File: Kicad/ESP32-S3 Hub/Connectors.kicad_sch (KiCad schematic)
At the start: 23 parts, among them J1 1.27mm 3pin socket, J10 1.27mm 3pin socket, J11 7 pin FPC 0.3mm Panasonic Y3b, J12 1.27mm 3pin socket, J13 TE 3-2363961-0 receptacle, J14 TE 3-2363962-0 Connector, J16 TE 3-2363961-0 receptacle, J17 TE 3-2363962-0 Connector, J2 1.27mm 3pin socket, J21 1.27mm 4 pin socket, J22 1.27mm 4 pin header, J3 7 pin FPC 0.3mm Panasonic Y3b, J4 1.27mm 3pin socket, J5 7 pin FPC 0.3mm Panasonic Y3b, J6 1.27mm 3pin socket, J7 1.27mm 3pin socket, J8 7 pin FPC 0.3mm Panasonic Y3b, J9 1.27mm 3pin socket

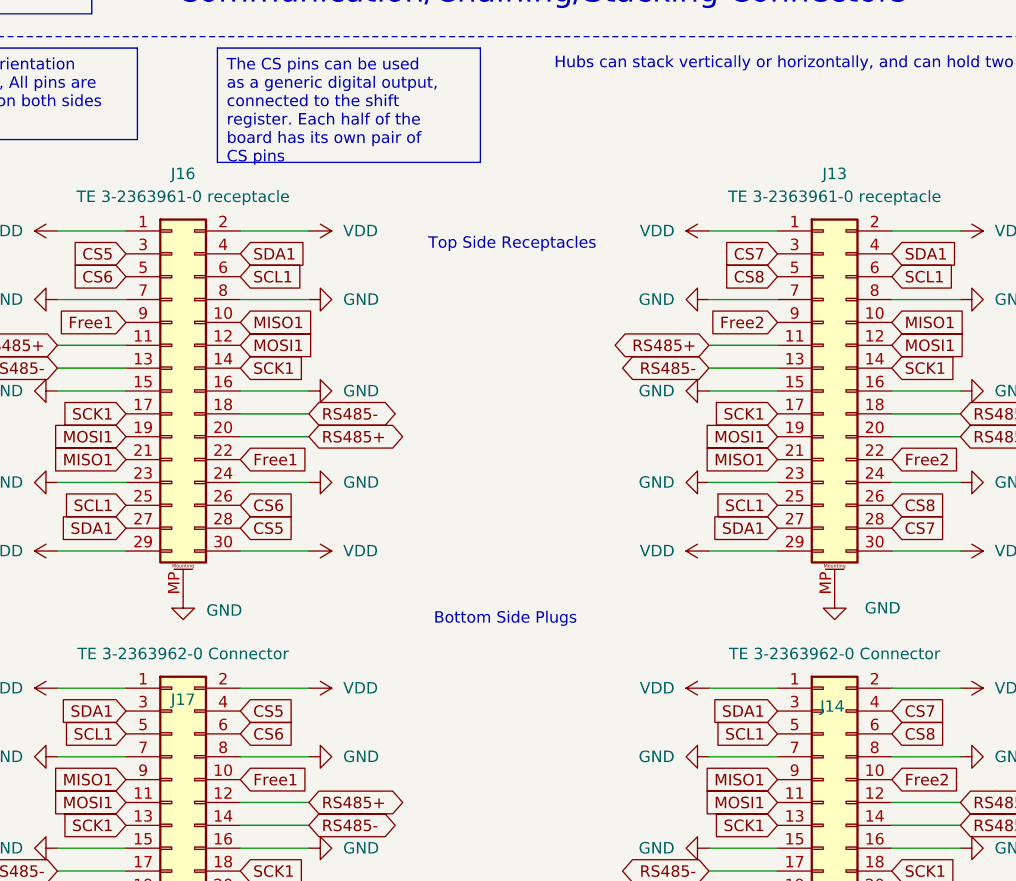
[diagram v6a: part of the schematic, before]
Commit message: Swapped header logical numbers
I realized my numbering scheme was off with the actual board layout. So in the schematic I swapped the connectors without rewiring so that the numbers are more logical. CS7, CS8, and Free2 are now for the top mezzanine connector, which is closer to the pins on the chips. It also falls in line with my bottom up numbering scheme.
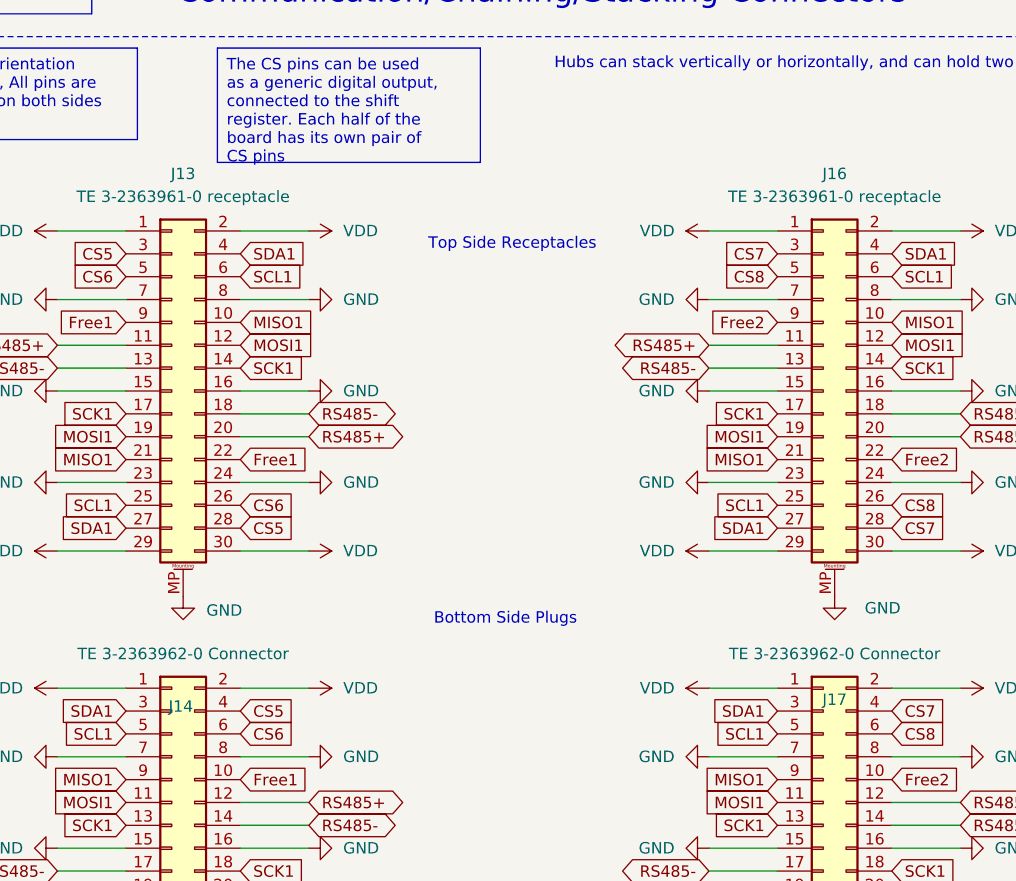
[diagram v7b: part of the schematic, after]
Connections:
- net CS5: now also J13.28 (Pin_28), J13.3 (Pin_3), J14.27 (Pin_27), J14.4 (Pin_4); no longer J16.28 (Pin_28), J16.3 (Pin_3), J17.27 (Pin_27), J17.4 (Pin_4)
- net CS6: now also J13.26 (Pin_26), J13.5 (Pin_5), J14.25 (Pin_25), J14.6 (Pin_6); no longer J16.26 (Pin_26), J16.5 (Pin_5), J17.25 (Pin_25), J17.6 (Pin_6)
- net CS7: now also J16.28 (Pin_28), J16.3 (Pin_3), J17.27 (Pin_27), J17.4 (Pin_4); no longer J13.28 (Pin_28), J13.3 (Pin_3), J14.27 (Pin_27), J14.4 (Pin_4)
- net CS8: now also J16.26 (Pin_26), J16.5 (Pin_5), J17.25 (Pin_25), J17.6 (Pin_6); no longer J13.26 (Pin_26), J13.5 (Pin_5), J14.25 (Pin_25), J14.6 (Pin_6)
- net Free1: now also J13.22 (Pin_22), J13.9 (Pin_9), J14.10 (Pin_10), J14.21 (Pin_21); no longer J16.22 (Pin_22), J16.9 (Pin_9), J17.10 (Pin_10), J17.21 (Pin_21)
- net Free2: now also J16.22 (Pin_22), J16.9 (Pin_9), J17.10 (Pin_10), J17.21 (Pin_21); no longer J13.22 (Pin_22), J13.9 (Pin_9), J14.10 (Pin_10), J14.21 (Pin_21)
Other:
- moved on the sheet: J13, J14, J16, J17
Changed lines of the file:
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@@
+	(symbol
+		(lib_id "Connector_Generic_MountingPin:Conn_02x15_Odd_Even_MountingPin")
+		(at 173.99 142.24 0)
+		(unit 1)
+		(exclude_from_sim no)
+		(in_bom yes)
+		(on_board yes)
+		(dnp no)
+		(property "Reference" "J14"
+			(at 175.006 126.492 0)
+			(effects
+				(font
+					(size 1.27 1.27)
+				)
+			)
+		)
+		(property "Value" "TE 3-2363962-0 Connector"
+			(at 175.26 120.65 0)
+			(effects
+				(font
+					(size 1.27 1.27)
+				)
+			)
+		)
+		(property "Footprint" "custom_testpoints:TE_mezzanine_conn_3-2363962-0"
+			(at 173.99 142.24 0)
+			(effects
+				(font
+					(size 1.27 1.27)
+				)
+				(hide yes)
+			)
+		)
+		(property "Datasheet" "~"
+			(at 173.99 142.24 0)
+			(effects
+				(font
+					(size 1.27 1.27)
+				)
+				(hide yes)
+			)
+		)
+		(property "Description" "Generic connectable mounting pin connector, double row, 02x15, odd/even pin numbering scheme (row 1 odd numbers, row 2 even numbers), script generated (kicad-library-utils/schlib/autogen/connector/)"
+			(at 173.99 142.24 0)
+			(effects
+				(font
+					(size 1.27 1.27)
+				)
+				(hide yes)
+			)
+		)
+		(pin "28"
+		)
+		(pin "21"
+		)
+		(pin "25"
+		)
+		(pin "5"
+		)
+		(pin "17"
+		)
+		(pin "6"
+		)
+		(pin "14"
+		)
+		(pin "2"
+		)
+		(pin "24"
+		)
+		(pin "8"
+		)
+		(pin "30"
+		)
+		(pin "23"
+		)
+		(pin "16"
+		)
+		(pin "19"
+		)
+		(pin "22"
+		)
+		(pin "7"
+		)
+		(pin "3"
+		)
+		(pin "9"
+		)
+		(pin "MP"
+		)
+		(pin "4"
+		)
+		(pin "27"
+		)
+		(pin "29"
+		)
+		(pin "26"
+		)
+		(pin "18"
+		)
+		(pin "20"
+		)
+		(pin "13"
+		)
+		(pin "10"
+		)
+		(pin "12"
+		)
+		(pin "11"
+		)
+		(pin "1"
+		)
+		(pin "15"
+		)
+		(instances
+			(project "ESP32-S3 Hub"
+				(path "/a8c80fba-3bca-4358-b5bb-9ebf9383c658/e098af34-1b04-4f22-87f1-2a3ef3b390de"
+					(reference "J14")
+					(unit 1)
+				)
+			)
+		)
+	)
+	(symbol
+		(lib_id "Device:R_Small")
+		(at 69.85 97.79 0)
+		(unit 1)
+		(exclude_from_sim no)
+		(in_bom yes)
+		(on_board yes)
+		(dnp no)
+		(property "Reference" "R19"
+			(at 71.12 101.346 0)
+			(effects
+				(font
+					(size 1.27 1.27)
+				)
+			)
+		)
+		(property "Value" "10k"
+			(at 66.548 98.044 0)
+			(effects
+				(font
+					(size 1.27 1.27)
+				)
+			)
+		)
+		(property "Footprint" "Resistor_SMD:R_0402_1005Metric"
+			(at 69.85 97.79 0)
+			(effects
+				(font
+					(size 1.27 1.27)
+				)
+				(hide yes)
+			)
+		)
+		(property "Datasheet" "~"
+			(at 69.85 97.79 0)
+			(effects
+				(font
+					(size 1.27 1.27)
+				)
+				(hide yes)
+			)
+		)
+		(property "Description" "Resistor, small symbol"
+			(at 69.85 97.79 0)
+			(effects
+				(font
+					(size 1.27 1.27)
+				)
+				(hide yes)
+			)
+		)
+		(pin "2"
+		)
+		(pin "1"
+		)
+		(instances
+			(project "ESP32-S3 Hub"
+				(path "/a8c80fba-3bca-4358-b5bb-9ebf9383c658/e098af34-1b04-4f22-87f1-2a3ef3b390de"
+					(reference "R19")
+					(unit 1)
+				)
+			)
+		)
+	)
 	(symbol
 		(lib_id "Connector_Generic_MountingPin:Conn_02x15_Odd_Even_MountingPin")
@@
 		(on_board yes)
 		(dnp no)
-		(property "Reference" "J14"
-			(at 247.396 126.492 0)
+		(property "Reference" "J17"
+			(at 247.65 125.73 0)
 			(effects
 				(font
@@
 		(property "Description" "Generic connectable mounting pin connector, double row, 02x15, odd/even pin numbering scheme (row 1 odd numbers, row 2 even numbers), script generated (kicad-library-utils/schlib/autogen/connector/)"
 			(at 246.38 142.24 0)
-			(effects
-				(font
-					(size 1.27 1.27)
-				)
-				(hide yes)
-			)
-		)
-		(pin "28"
-		)
-		(pin "21"
-		)
-		(pin "25"
-		)
-		(pin "5"
-		)
-		(pin "17"
-		)
-		(pin "6"
-		)
-		(pin "14"
-		)
-		(pin "2"
-		)
-		(pin "24"
-		)
-		(pin "8"
-		)
-		(pin "30"
-		)
-		(pin "23"
-		)
-		(pin "16"
-		)
-		(pin "19"
-		)
-		(pin "22"
-		)
-		(pin "7"
-		)
-		(pin "3"
-		)
-		(pin "9"
-		)
-		(pin "MP"
-		)
-		(pin "4"
-		)
-		(pin "27"
-		)
-		(pin "29"
-		)
-		(pin "26"
-		)
-		(pin "18"
-		)
-		(pin "20"
-		)
-		(pin "13"
-		)
-		(pin "10"
-		)
-		(pin "12"
-		)
-		(pin "11"
-		)
-		(pin "1"
-		)
-		(pin "15"
-		)
-		(instances
-			(project "ESP32-S3 Hub"
-				(path "/a8c80fba-3bca-4358-b5bb-9ebf9383c658/e098af34-1b04-4f22-87f1-2a3ef3b390de"
-					(reference "J14")
-					(unit 1)
-				)
-			)
-		)
-	)
-	(symbol
-		(lib_id "Device:R_Small")
-		(at 69.85 97.79 0)
-		(unit 1)
-		(exclude_from_sim no)
-		(in_bom yes)
-		(on_board yes)
-		(dnp no)
-		(property "Reference" "R19"
-			(at 71.12 101.346 0)
-			(effects
-				(font
-					(size 1.27 1.27)
-				)
-			)
-		)
-		(property "Value" "10k"
-			(at 66.548 98.044 0)
-			(effects
-				(font
-					(size 1.27 1.27)
-				)
-			)
-		)
-		(property "Footprint" "Resistor_SMD:R_0402_1005Metric"
-			(at 69.85 97.79 0)
-			(effects
-				(font
-					(size 1.27 1.27)
-				)
-				(hide yes)
-			)
-		)
-		(property "Datasheet" "~"
-			(at 69.85 97.79 0)
-			(effects
-				(font
-					(size 1.27 1.27)
-				)
-				(hide yes)
-			)
-		)
-		(property "Description" "Resistor, small symbol"
-			(at 69.85 97.79 0)
-			(effects
-				(font
-					(size 1.27 1.27)
-				)
-				(hide yes)
-			)
-		)
-		(pin "2"
-		)
-		(pin "1"
-		)
-		(instances
-			(project "ESP32-S3 Hub"
-				(path "/a8c80fba-3bca-4358-b5bb-9ebf9383c658/e098af34-1b04-4f22-87f1-2a3ef3b390de"
-					(reference "R19")
-					(unit 1)
-				)
-			)
-		)
-	)
-	(symbol
-		(lib_id "Connector_Generic_MountingPin:Conn_02x15_Odd_Even_MountingPin")
-		(at 173.99 142.24 0)
-		(unit 1)
-		(exclude_from_sim no)
-		(in_bom yes)
-		(on_board yes)
-		(dnp no)
-		(property "Reference" "J17"
-			(at 175.26 125.73 0)
-			(effects
-				(font
-					(size 1.27 1.27)
-				)
-			)
-		)
-		(property "Value" "TE 3-2363962-0 Connector"
-			(at 175.26 120.65 0)
-			(effects
-				(font
-					(size 1.27 1.27)
-				)
-			)
-		)
-		(property "Footprint" "custom_testpoints:TE_mezzanine_conn_3-2363962-0"
-			(at 173.99 142.24 0)
-			(effects
-				(font
-					(size 1.27 1.27)
-				)
-				(hide yes)
-			)
-		)
-		(property "Datasheet" "~"
-			(at 173.99 142.24 0)
-			(effects
-				(font
-					(size 1.27 1.27)
-				)
-				(hide yes)
-			)
-		)
-		(property "Description" "Generic connectable mounting pin connector, double row, 02x15, odd/even pin numbering scheme (row 1 odd numbers, row 2 even numbers), script generated (kicad-library-utils/schlib/autogen/connector/)"
-			(at 173.99 142.24 0)
 			(effects
 				(font
@@
 	(symbol
 		(lib_id "Connector_Generic_MountingPin:Conn_02x15_Odd_Even_MountingPin")
-		(at 246.38 91.44 0)
+		(at 173.99 91.44 0)
 		(unit 1)
 		(exclude_from_sim no)
@@
 		(fields_autoplaced yes)
 		(property "Reference" "J13"
-			(at 247.65 67.31 0)
+			(at 175.26 67.31 0)
 			(effects
 				(font
@@
 		)
 		(property "Value" "TE 3-2363961-0 receptacle"
-			(at 247.65 69.85 0)
+			(at 175.26 69.85 0)
 			(effects
 				(font
@@
 		)
 		(property "Footprint" "custom_testpoints:TE_mezzanine_rec_3-2363961-0"
-			(at 246.38 91.44 0)
+			(at 173.99 91.44 0)
 			(effects
 				(font
@@
 		)
 		(property "Datasheet" "~"
-			(at 246.38 91.44 0)
+			(at 173.99 91.44 0)
 			(effects
 				(font
@@
 		)
 		(property "Description" "Generic connectable mounting pin connector, double row, 02x15, odd/even pin numbering scheme (row 1 odd numbers, row 2 even numbers), script generated (kicad-library-utils/schlib/autogen/connector/)"
-			(at 246.38 91.44 0)
+			(at 173.99 91.44 0)
 			(effects
 				(font
@@
 	(symbol
 		(lib_id "Connector_Generic_MountingPin:Conn_02x15_Odd_Even_MountingPin")
-		(at 173.99 91.44 0)
+		(at 246.38 91.44 0)
 		(unit 1)
 		(exclude_from_sim no)
@@
 		(fields_autoplaced yes)
 		(property "Reference" "J16"
-			(at 175.26 67.31 0)
+			(at 247.65 67.31 0)
 			(effects
 				(font
@@
 		)
 		(property "Value" "TE 3-2363961-0 receptacle"
-			(at 175.26 69.85 0)
+			(at 247.65 69.85 0)
 			(effects
 				(font
@@
 		)
 		(property "Footprint" "custom_testpoints:TE_mezzanine_rec_3-2363961-0"
-			(at 173.99 91.44 0)
+			(at 246.38 91.44 0)
 			(effects
 				(font
@@
 		)
 		(property "Datasheet" "~"
-			(at 173.99 91.44 0)
+			(at 246.38 91.44 0)
 			(effects
 				(font
@@
 		)
 		(property "Description" "Generic connectable mounting pin connector, double row, 02x15, odd/even pin numbering scheme (row 1 odd numbers, row 2 even numbers), script generated (kicad-library-utils/schlib/autogen/connector/)"
-			(at 173.99 91.44 0)
-			(effects
-				(font
+			(at 246.38 91.44 0)
+			(effects
+				(font

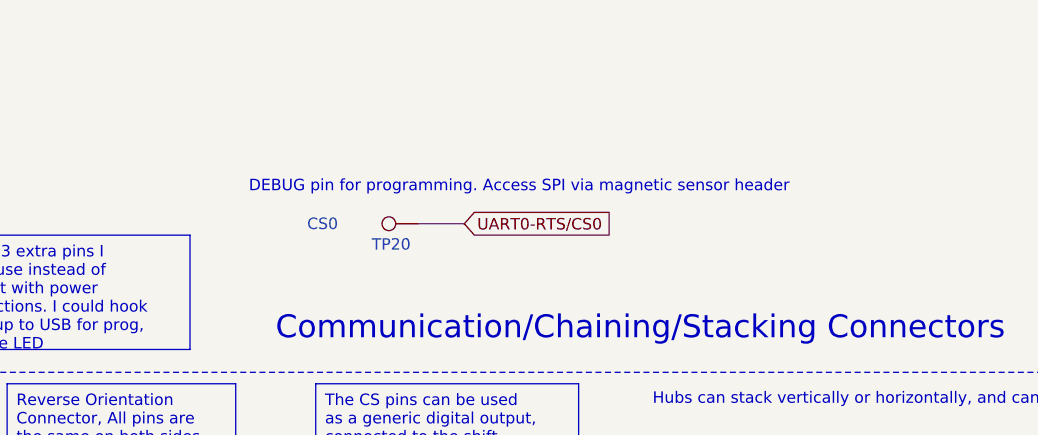
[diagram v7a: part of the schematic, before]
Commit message: Finished basic routing
Now I have to fix some things to try and reduce crosstalk, and improve signal integrity. The likelihood of me being able to completely fix it is low, due to limited space. I also have to run the DRC, and fix the silkscreen.
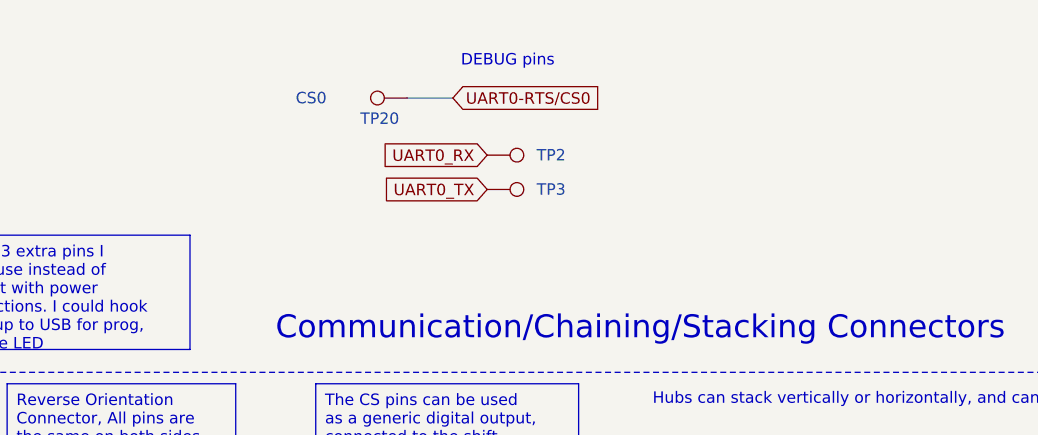
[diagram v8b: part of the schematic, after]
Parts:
- added TP2, TP3: ~, TestPoint:TestPoint_Pad_D1.0mm, symbol Connector:TestPoint
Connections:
- new net UART0_RX: TP2.1
- new net UART0_TX: TP3.1
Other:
- note added: "DEBUG pins"
- note removed: "DEBUG pin for programming. Access SPI via magnetic sensor header"
- moved on the sheet: TP20
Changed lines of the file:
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@@
 	(wire
 		(pts
-			(xy 195.58 35.56) (xy 190.5 35.56)
+			(xy 194.31 21.59) (xy 189.23 21.59)
 		)
 		(stroke
@@
 		)
 	)
-	(text "DEBUG pin for programming. Access SPI via magnetic sensor header"
+	(text "DEBUG pins"
 		(exclude_from_sim no)
-		(at 201.676 31.496 0)
+		(at 200.406 17.526 0)
 		(effects
 			(font
@@
 		)
 	)
+	(global_label "UART0_RX"
+		(shape input)
+		(at 198.12 27.94 180)
+		(fields_autoplaced yes)
+		(effects
+			(font
+				(size 1.27 1.27)
+			)
+			(justify right)
+		)
+		(property "Intersheetrefs" "${INTERSHEET_REFS}"
+			(at 185.8215 27.94 0)
+			(effects
+				(font
+					(size 1.27 1.27)
+				)
+				(justify right)
+				(hide yes)
+			)
+		)
+	)
 	(global_label "SCL1"
 		(shape input)
@@
 		)
 	)
+	(global_label "UART0_TX"
+		(shape input)
+		(at 198.12 31.75 180)
+		(fields_autoplaced yes)
+		(effects
+			(font
+				(size 1.27 1.27)
+			)
+			(justify right)
+		)
+		(property "Intersheetrefs" "${INTERSHEET_REFS}"
+			(at 186.1239 31.75 0)
+			(effects
+				(font
+					(size 1.27 1.27)
+				)
+				(justify right)
+				(hide yes)
+			)
+		)
+	)
 	(global_label "RS485-"
 		(shape bidirectional)
@@
 	(global_label "UART0-RTS{slash}CS0"
 		(shape input)
-		(at 195.58 35.56 0)
+		(at 194.31 21.59 0)
 		(fields_autoplaced yes)
 		(effects
@@
 		)
 		(property "Intersheetrefs" "${INTERSHEET_REFS}"
-			(at 214.4704 35.56 0)
+			(at 213.2004 21.59 0)
 			(effects
 				(font
@@
 	(symbol
 		(lib_id "Connector:TestPoint")
-		(at 190.5 35.56 90)
+		(at 189.23 21.59 90)
 		(unit 1)
 		(exclude_from_sim no)
@@
 		(dnp no)
 		(property "Reference" "TP20"
-			(at 187.452 37.846 90)
+			(at 186.182 23.876 90)
 			(effects
 				(font
@@
 		)
 		(property "Value" "CS0"
-			(at 179.832 35.56 90)
+			(at 178.562 21.59 90)
 			(effects
 				(font
@@
 		)
 		(property "Footprint" "TestPoint:TestPoint_Pad_D1.0mm"
-			(at 190.5 30.48 0)
+			(at 189.23 16.51 0)
 			(effects
 				(font
@@
 		)
 		(property "Datasheet" "~"
-			(at 190.5 30.48 0)
+			(at 189.23 16.51 0)
 			(effects
 				(font
@@
 		)
 		(property "Description" "test point"
-			(at 190.5 35.56 0)
+			(at 189.23 21.59 0)
 			(effects
 				(font
@@
 	)
 	(symbol
+		(lib_id "Connector:TestPoint")
+		(at 198.12 31.75 270)
+		(unit 1)
+		(exclude_from_sim no)
+		(in_bom no)
+		(on_board yes)
+		(dnp no)
+		(property "Reference" "TP3"
+			(at 205.232 31.75 90)
+			(effects
+				(font
+					(size 1.27 1.27)
+				)
+			)
+		)
+		(property "Value" "~"
+			(at 207.01 32.004 90)
+			(effects
+				(font
+					(size 1.27 1.27)
+				)
+			)
+		)
+		(property "Footprint" "TestPoint:TestPoint_Pad_D1.0mm"
+			(at 198.12 36.83 0)
+			(effects
+				(font
+					(size 1.27 1.27)
+				)
+				(hide yes)
+			)
+		)
+		(property "Datasheet" "~"
+			(at 198.12 36.83 0)
+			(effects
+				(font
+					(size 1.27 1.27)
+				)
+				(hide yes)
+			)
+		)
+		(property "Description" "test point"
+			(at 198.12 31.75 0)
+			(effects
+				(font
+					(size 1.27 1.27)
+				)
+				(hide yes)
+			)
+		)
+		(pin "1"
+		)
+		(instances
+			(project "ESP32-S3 Hub"
+				(path "/a8c80fba-3bca-4358-b5bb-9ebf9383c658/e098af34-1b04-4f22-87f1-2a3ef3b390de"
+					(reference "TP3")
+					(unit 1)
+				)
+			)
+		)
+	)
+	(symbol
 		(lib_id "power:GND")
 		(at 162.56 187.96 90)
@@
 					(unit 1)
 				)
+			)
+		)
+	)
+	(symbol
+		(lib_id "Connector:TestPoint")
+		(at 198.12 27.94 270)
+		(unit 1)
+		(exclude_from_sim no)
+		(in_bom no)
+		(on_board yes)
+		(dnp no)
+		(property "Reference" "TP2"
+			(at 205.232 27.94 90)
+			(effects
+				(font
+					(size 1.27 1.27)
+				)
+			)
+		)
+		(property "Value" "~"
+			(at 207.01 28.194 90)
+			(effects
+				(font
+					(size 1.27 1.27)
+				)
+			)
+		)
+		(property "Footprint" "TestPoint:TestPoint_Pad_D1.0mm"
+			(at 198.12 33.02 0)
+			(effects
+				(font
+					(size 1.27 1.27)
+				)
+				(hide yes)
+			)
+		)
+		(property "Datasheet" "~"
+			(at 198.12 33.02 0)
+			(effects
+				(font
+					(size 1.27 1.27)
+				)
+				(hide yes)
+			)
+		)
+		(property "Description" "test point"
+			(at 198.12 27.94 0)
+			(effects
+				(font
+					(size 1.27 1.27)
+				)
+				(hide yes)
+			)
+		)
+		(pin "1"
+		)
+		(instances
+			(project "ESP32-S3 Hub"
+				(path "/a8c80fba-3bca-4358-b5bb-9ebf9383c658/e098af34-1b04-4f22-87f1-2a3ef3b390de"
+					(reference "TP2")
+					(unit 1)
+				)
